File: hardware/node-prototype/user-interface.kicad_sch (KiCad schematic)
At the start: 0 parts

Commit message: WIP on user interface
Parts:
- added D1: White, symbol Device:LED
- added D2, D7: Red, symbol Device:LED
- added D5: Green, symbol Device:LED
- added D8: Yellow, symbol Device:LED
- added Q3: 2N7002, Package_TO_SOT_SMD:SOT-23, symbol Transistor_FET:2N7002
- added R33, R34: 10k, symbol Device:R
- added R35, R42, R44: R, symbol Device:R
- added R36, R43: 130R, symbol Device:R
- added R37: 330R, symbol Device:R
- added R38: 220k, symbol Device:R
- added SW1: BOOT0, symbol Switch:SW_Push
- added SW2: ~{RESET}, symbol Switch:SW_Push
- added SW3: USER_BTN, symbol Switch:SW_Push
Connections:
- new net: D1.2 (A), R35.2
- new net: R37.2, R38.1, SW3.1
- new net: D2.2 (A), R36.2
- new net: D8.1 (K), R44.1
- new net: D5.1 (K), R42.1
- new net: Q3.3 (D), R43.2
- new net: D7.1 (K), R43.1
- new net BOOT0: R33.1, SW1.1
- new net GND: D1.1 (K), D2.1 (K), Q3.2 (S), R33.2, R38.2, R42.2, R44.2, SW2.2
- new net POE_5V: D5.2 (A)
- new net USB_VBUS: D8.2 (A)
- new net USER_BTN: R37.1
- new net USER_LED_RED: R36.1
- new net USER_LED_WHITE: R35.1
- new net VDD: D7.2 (A), R34.1, SW1.2, SW3.2
- new net ~{MIC_SHDN}: Q3.1 (G)
- new net ~{RESET}: R34.2, SW2.1
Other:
- note removed: "TODO: Add buttons and LEDs"

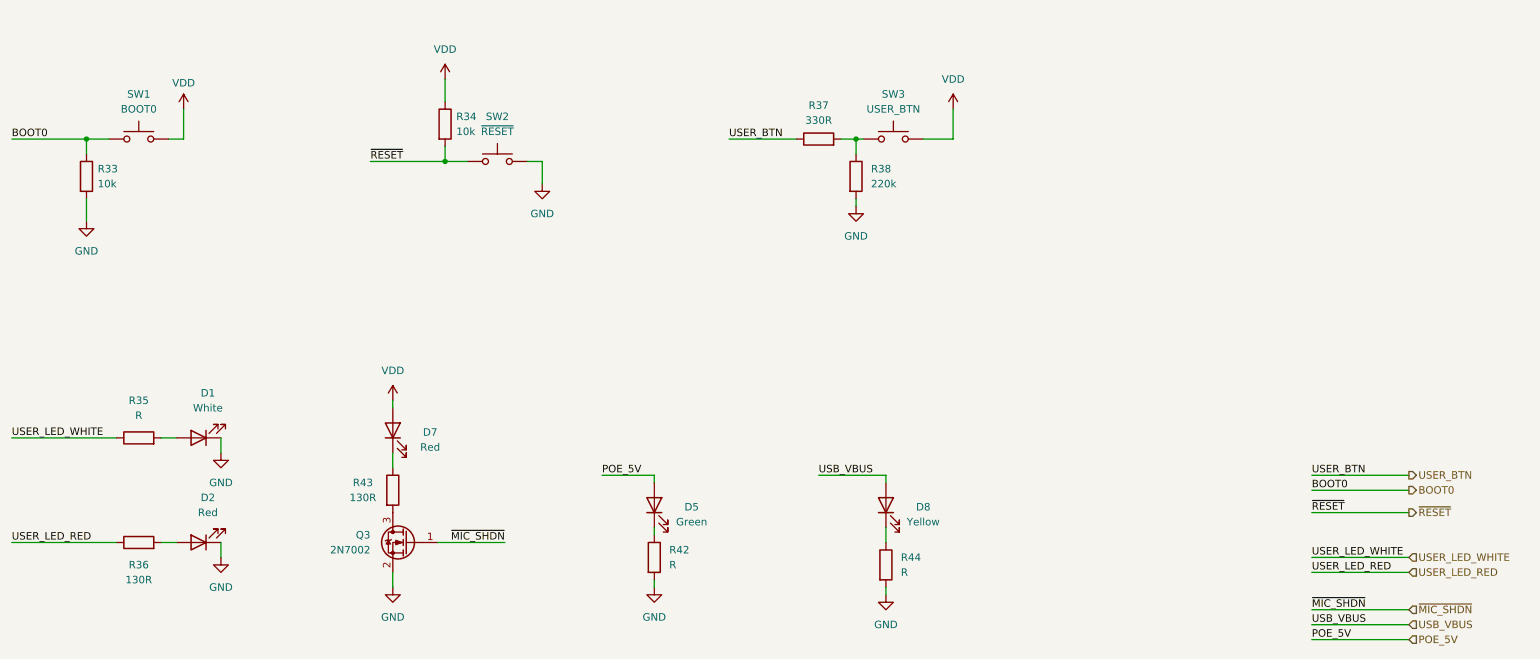
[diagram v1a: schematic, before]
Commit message: Plug schematic together
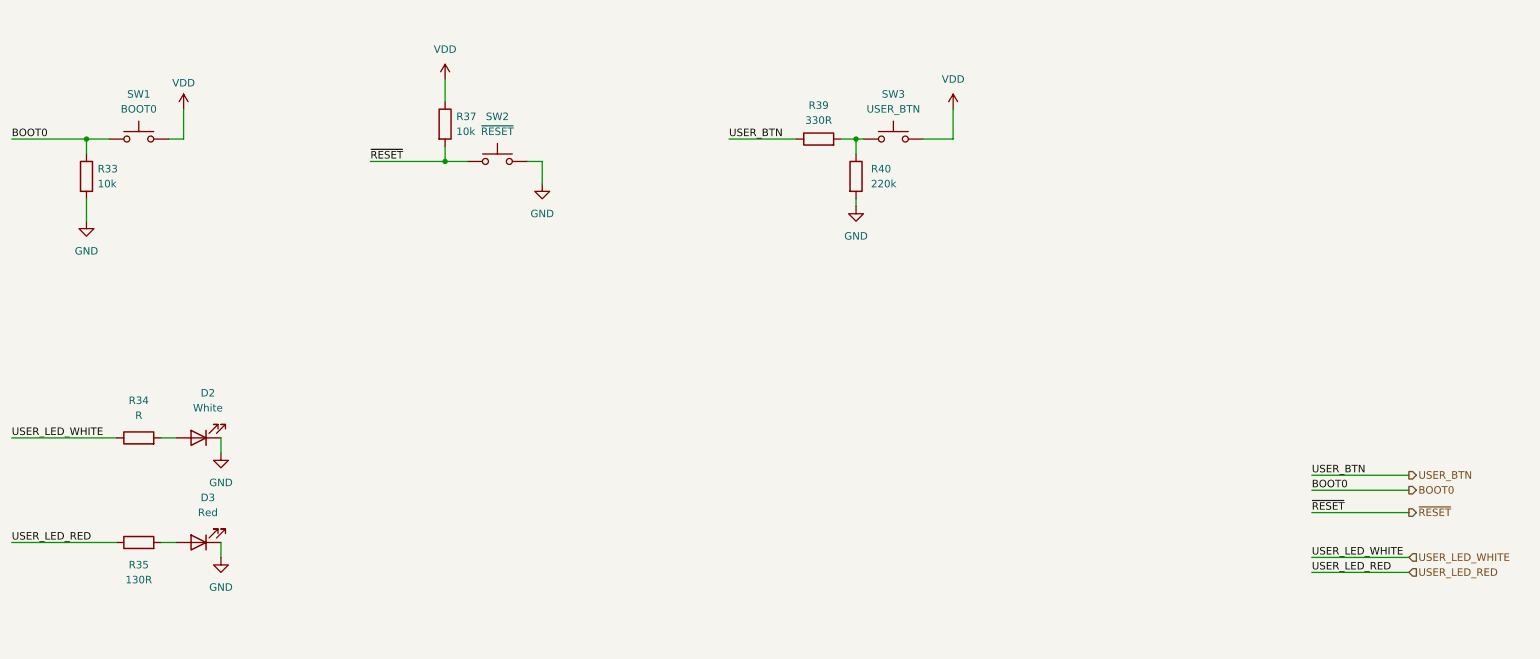
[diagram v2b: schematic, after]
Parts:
- removed D5: Green, symbol Device:LED
- removed D7: Red, symbol Device:LED
- removed D8: Yellow, symbol Device:LED
- removed Q3: 2N7002, Package_TO_SOT_SMD:SOT-23, symbol Transistor_FET:2N7002
- removed R42, R44: R, symbol Device:R
- removed R43: 130R, symbol Device:R
- D2: renamed from D1; footprint (none) -> LED_SMD:LED_0603_1608Metric
- D3: renamed from D2; footprint (none) -> LED_SMD:LED_0603_1608Metric
- R33: footprint (none) -> Resistor_SMD:R_0603_1608Metric
- R34: renamed from R35; footprint (none) -> Resistor_SMD:R_0603_1608Metric
- R35: renamed from R36; footprint (none) -> Resistor_SMD:R_0603_1608Metric
- R37: renamed from R34; footprint (none) -> Resistor_SMD:R_0603_1608Metric
- R39: renamed from R37; footprint (none) -> Resistor_SMD:R_0603_1608Metric
- R40: renamed from R38; footprint (none) -> Resistor_SMD:R_0603_1608Metric
- SW1, SW2, SW3: footprint (none) -> MYBSP01201ABF_MYBSP00502ABF:TS-1187A-B-A-B

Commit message: Design PPS output, fix LEDs and their resistors
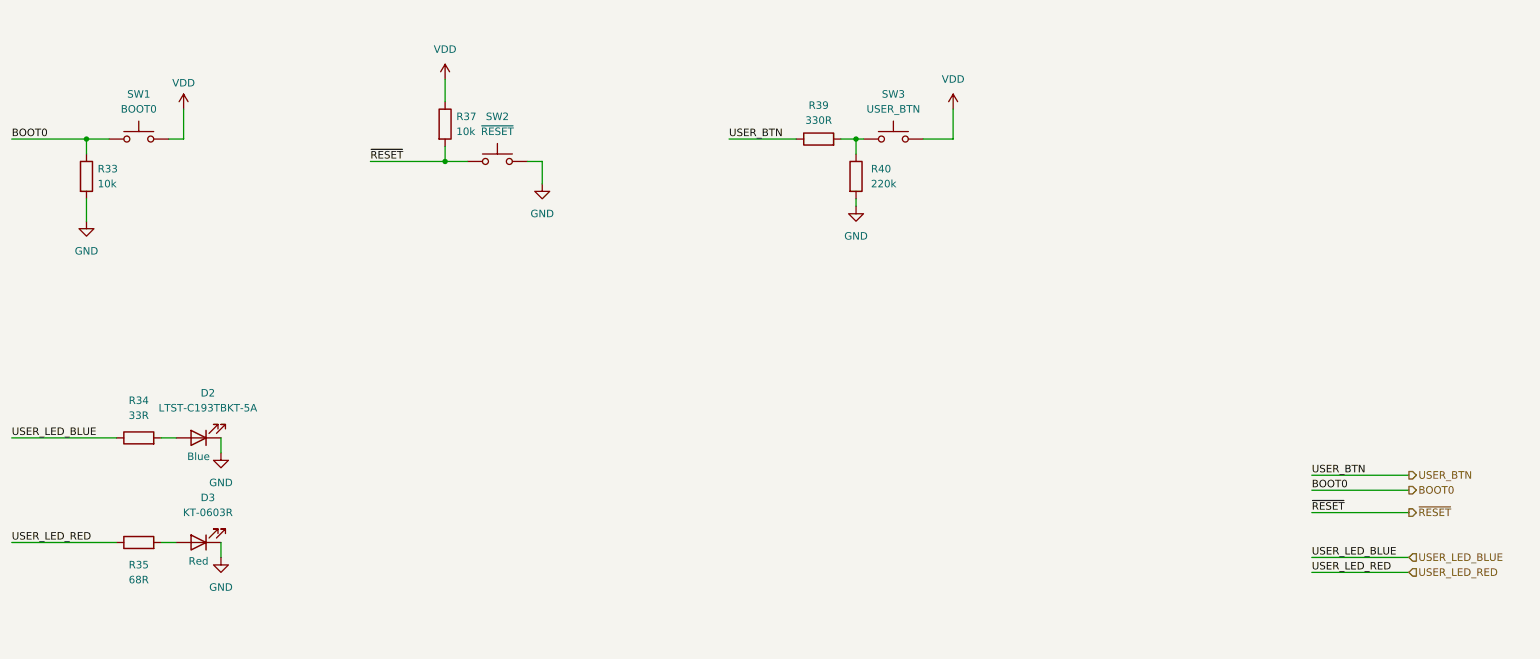
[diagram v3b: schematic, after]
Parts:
- D2: value White -> LTST-C193TBKT-5A; Color (none) -> Blue
- D3: value Red -> KT-0603R; Color (none) -> Red
- R34: value R -> 33R
- R35: value 130R -> 68R
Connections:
- net USER_LED_WHITE renamed USER_LED_BLUE
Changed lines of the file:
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@@
     (effects (font (size 1.27 1.27)) (justify left bottom))
   )
-  (label "USER_LED_WHITE" (at 30.48 106.68 0) (fields_autoplaced)
+  (label "USER_LED_BLUE" (at 30.48 106.68 0) (fields_autoplaced)
     (effects (font (size 1.27 1.27)) (justify left bottom))
   )
@@
     (effects (font (size 1.27 1.27)) (justify left bottom))
   )
-  (label "USER_LED_WHITE" (at 251.46 127 0) (fields_autoplaced)
+  (label "USER_LED_BLUE" (at 251.46 127 0) (fields_autoplaced)
     (effects (font (size 1.27 1.27)) (justify left bottom))
   )
@@
     (effects (font (size 1.27 1.27)) (justify left))
   )
-  (hierarchical_label "USER_LED_WHITE" (shape input) (at 267.97 127 0) (fields_autoplaced)
+  (hierarchical_label "USER_LED_BLUE" (shape input) (at 267.97 127 0) (fields_autoplaced)
     (effects (font (size 1.27 1.27)) (justify left))
   )
@@
       (effects (font (size 1.27 1.27)))
     )
-    (property "Value" "R" (at 52.07 102.87 90)
+    (property "Value" "33R" (at 52.07 102.87 90)
       (effects (font (size 1.27 1.27)))
     )
@@
   )
   (symbol (lib_id "Device:LED") (at 62.23 124.46 180) (unit 1)
-    (in_bom yes) (on_board yes) (dnp no) (fields_autoplaced)
+    (in_bom yes) (on_board yes) (dnp no)
     (property "Reference" "D3" (at 63.8175 116.84 0)
       (effects (font (size 1.27 1.27)))
     )
-    (property "Value" "Red" (at 63.8175 119.38 0)
+    (property "Value" "KT-0603R" (at 63.8175 119.38 0)
       (effects (font (size 1.27 1.27)))
     )
@@
     (property "Datasheet" "~" (at 62.23 124.46 0)
       (effects (font (size 1.27 1.27)) hide)
+    )
+    (property "Color" "Red" (at 62.23 127.635 0)
+      (effects (font (size 1.27 1.27)))
     )
     (pin "1")
@@
       (effects (font (size 1.27 1.27)))
     )
-    (property "Value" "130R" (at 52.07 130.81 90)
+    (property "Value" "68R" (at 52.07 130.81 90)
       (effects (font (size 1.27 1.27)))
     )
@@
   )
   (symbol (lib_id "Device:LED") (at 62.23 106.68 180) (unit 1)
-    (in_bom yes) (on_board yes) (dnp no) (fields_autoplaced)
+    (in_bom yes) (on_board yes) (dnp no)
     (property "Reference" "D2" (at 63.8175 99.06 0)
       (effects (font (size 1.27 1.27)))
     )
-    (property "Value" "White" (at 63.8175 101.6 0)
+    (property "Value" "LTST-C193TBKT-5A" (at 63.8175 101.6 0)
       (effects (font (size 1.27 1.27)))
     )
@@
       (effects (font (size 1.27 1.27)) hide)
     )
-    (property "Field4" "" (at 62.23 106.68 0)
-      (effects (font (size 1.27 1.27)) hide)
-    )
-    (pin "1")
+    (property "Color" "Blue" (at 62.23 109.855 0)
+      (effects (font (size 1.27 1.27)))
+    )
+    (pin "1")

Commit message: Double check schematic
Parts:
- added U4: SRV05-4, Package_TO_SOT_SMD:SOT-23-6, symbol Power_Protection:SRV05-4
- R34: value 33R -> 100R
- R35: value 68R -> 270R
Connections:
- net BOOT0: now also U4.1 (IO1)
- net GND: now also U4.2 (VN)
- net USER_BTN: now also U4.4 (IO3)
- net VDD: now also U4.5 (VP)
- net ~{RESET}: now also U4.3 (IO2)
- no-connect marks 0 -> 1
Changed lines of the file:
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@@
   (junction (at 173.99 55.88) (diameter 0) (color 0 0 0 0)
   )
+  (no_connect (at 243.84 59.69))
+  (wire (pts (xy 231.14 69.85) (xy 231.14 71.12))
+    (stroke (width 0) (type default))
+  )
   (wire (pts (xy 66.04 109.22) (xy 66.04 106.68))
     (stroke (width 0) (type default))
@@
     (stroke (width 0) (type default))
   )
+  (wire (pts (xy 212.09 54.61) (xy 218.44 54.61))
+    (stroke (width 0) (type default))
+  )
   (wire (pts (xy 104.14 57.15) (xy 104.14 59.69))
     (stroke (width 0) (type default))
@@
     (stroke (width 0) (type default))
   )
+  (wire (pts (xy 231.14 40.64) (xy 231.14 44.45))
+    (stroke (width 0) (type default))
+  )
   (wire (pts (xy 55.88 106.68) (xy 58.42 106.68))
     (stroke (width 0) (type default))
@@
     (stroke (width 0) (type default))
   )
+  (wire (pts (xy 255.27 54.61) (xy 243.84 54.61))
+    (stroke (width 0) (type default))
+  )
   (wire (pts (xy 43.18 66.04) (xy 43.18 69.85))
     (stroke (width 0) (type default))
   )
+  (wire (pts (xy 212.09 59.69) (xy 218.44 59.69))
+    (stroke (width 0) (type default))
+  )
   (wire (pts (xy 59.69 50.8) (xy 59.69 55.88))
     (stroke (width 0) (type default))
@@
     (effects (font (size 1.27 1.27)) (justify left bottom))
   )
+  (label "BOOT0" (at 212.09 54.61 0) (fields_autoplaced)
+    (effects (font (size 1.27 1.27)) (justify left bottom))
+  )
   (label "BOOT0" (at 30.48 55.88 0) (fields_autoplaced)
     (effects (font (size 1.27 1.27)) (justify left bottom))
@@
     (effects (font (size 1.27 1.27)) (justify left bottom))
   )
+  (label "~{RESET}" (at 212.09 59.69 0) (fields_autoplaced)
+    (effects (font (size 1.27 1.27)) (justify left bottom))
+  )
   (label "USER_LED_RED" (at 251.46 129.54 0) (fields_autoplaced)
     (effects (font (size 1.27 1.27)) (justify left bottom))
@@
   (label "BOOT0" (at 251.46 115.57 0) (fields_autoplaced)
     (effects (font (size 1.27 1.27)) (justify left bottom))
+  )
+  (label "USER_BTN" (at 255.27 54.61 180) (fields_autoplaced)
+    (effects (font (size 1.27 1.27)) (justify right bottom))
   )
   (hierarchical_label "BOOT0" (shape output) (at 267.97 115.57 0) (fields_autoplaced)
@@
       (effects (font (size 1.27 1.27)))
     )
-    (property "Value" "33R" (at 52.07 102.87 90)
+    (property "Value" "100R" (at 52.07 102.87 90)
       (effects (font (size 1.27 1.27)))
     )
@@
         (path "/294f7425-8100-4c88-a430-3b04b29ed98a/01546861-6090-4f4c-8f1c-323aafea7461"
           (reference "#PWR052") (unit 1)
+        )
+      )
+    )
+  )
+  (symbol (lib_id "Power_Protection:SRV05-4") (at 231.14 57.15 0) (unit 1)
+    (in_bom yes) (on_board yes) (dnp no) (fields_autoplaced)
+    (property "Reference" "U4" (at 234.7661 41.91 0)
+      (effects (font (size 1.27 1.27)) (justify left))
+    )
+    (property "Value" "SRV05-4" (at 234.7661 44.45 0)
+      (effects (font (size 1.27 1.27)) (justify left))
+    )
+    (property "Footprint" "Package_TO_SOT_SMD:SOT-23-6" (at 248.92 68.58 0)
+      (effects (font (size 1.27 1.27)) hide)
+    )
+    (property "Datasheet" "http://www.onsemi.com/pub/Collateral/SRV05-4-D.PDF" (at 231.14 57.15 0)
+      (effects (font (size 1.27 1.27)) hide)
+    )
+    (pin "1")
+    (pin "2")
+    (pin "3")
+    (pin "4")
+    (pin "5")
+    (pin "6")
+    (instances
+      (project "node-prototype"
+        (path "/294f7425-8100-4c88-a430-3b04b29ed98a/83d2f1ea-2c2d-456e-b4de-3b699a617e5f"
+          (reference "U4") (unit 1)
+        )
+        (path "/294f7425-8100-4c88-a430-3b04b29ed98a/01546861-6090-4f4c-8f1c-323aafea7461"
+          (reference "U14") (unit 1)
         )
       )
@@
       (effects (font (size 1.27 1.27)))
     )
-    (property "Value" "68R" (at 52.07 130.81 90)
+    (property "Value" "270R" (at 52.07 130.81 90)
       (effects (font (size 1.27 1.27)))
     )
@@
     )
   )
+  (symbol (lib_id "power:VDD") (at 231.14 40.64 0) (unit 1)
+    (in_bom yes) (on_board yes) (dnp no) (fields_autoplaced)
+    (property "Reference" "#PWR088" (at 231.14 44.45 0)
+      (effects (font (size 1.27 1.27)) hide)
+    )
+    (property "Value" "VDD" (at 231.14 35.56 0)
+      (effects (font (size 1.27 1.27)))
+    )
+    (property "Footprint" "" (at 231.14 40.64 0)
+      (effects (font (size 1.27 1.27)) hide)
+    )
+    (property "Datasheet" "" (at 231.14 40.64 0)
+      (effects (font (size 1.27 1.27)) hide)
+    )
+    (pin "1")
+    (instances
+      (project "node-prototype"
+        (path "/294f7425-8100-4c88-a430-3b04b29ed98a/01546861-6090-4f4c-8f1c-323aafea7461"
+          (reference "#PWR088") (unit 1)
+        )
+      )
+    )
+  )
   (symbol (lib_id "Device:R") (at 43.18 62.23 0) (unit 1)
     (in_bom yes) (on_board yes) (dnp no) (fields_autoplaced)
@@
         )
       )
+    )
+  )
+  (symbol (lib_id "power:GND") (at 231.14 71.12 0) (unit 1)
+    (in_bom yes) (on_board yes) (dnp no) (fields_autoplaced)
+    (property "Reference" "#PWR089" (at 231.14 77.47 0)
+      (effects (font (size 1.27 1.27)) hide)
+    )
+    (property "Value" "GND" (at 231.14 76.2 0)
+      (effects (font (size 1.27 1.27)))
+    )
+    (property "Footprint" "" (at 231.14 71.12 0)
+      (effects (font (size 1.27 1.27)) hide)
+    )
+    (property "Datasheet" "" (at 231.14 71.12 0)
+      (effects (font (size 1.27 1.27)) hide)
+    )
+    (pin "1")
+    (instances
+      (project "node-prototype"
+        (path "/294f7425-8100-4c88-a430-3b04b29ed98a/01546861-6090-4f4c-8f1c-323aafea7461"
+          (reference "#PWR089") (unit 1)
+        )
+      )

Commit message: prepare for production
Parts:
- D2: now not fitted
- SW1: value BOOT0 -> TS-1187A-B-A-B
- SW2: value ~{RESET} -> TS-1187A-B-A-B
- SW3: value USER_BTN -> TS-1187A-B-A-B
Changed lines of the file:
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@@
       (effects (font (size 1.27 1.27)))
     )
-    (property "Value" "USER_BTN" (at 180.34 50.8 0)
+    (property "Value" "TS-1187A-B-A-B" (at 180.34 50.8 0)
       (effects (font (size 1.27 1.27)))
     )
@@
   )
   (symbol (lib_id "Device:LED") (at 62.23 106.68 180) (unit 1)
-    (in_bom yes) (on_board yes) (dnp no)
+    (in_bom yes) (on_board yes) (dnp yes)
     (property "Reference" "D2" (at 63.8175 99.06 0)
       (effects (font (size 1.27 1.27)))
@@
       (effects (font (size 1.27 1.27)))
     )
-    (property "Value" "BOOT0" (at 52.07 50.8 0)
+    (property "Value" "TS-1187A-B-A-B" (at 52.07 50.8 0)
       (effects (font (size 1.27 1.27)))
     )
@@
       (effects (font (size 1.27 1.27)))
     )
-    (property "Value" "~{RESET}" (at 113.03 54.61 0)
-      (effects (font (size 1.27 1.27)))
-    )
+    (property "Value" "TS-1187A-B-A-B" (at 113.03 54.61 0)
+      (effects (font (size 1.27 1.27)))
+    )
